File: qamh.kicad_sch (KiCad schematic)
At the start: 18 parts, among them J1 Eurorack_Power_16pin_Shrouded, J2 OUTPUT, J3 INPUT 1, J4 INPUT 2, J5 INPUT 3, J6 Conn_01x02_Pin

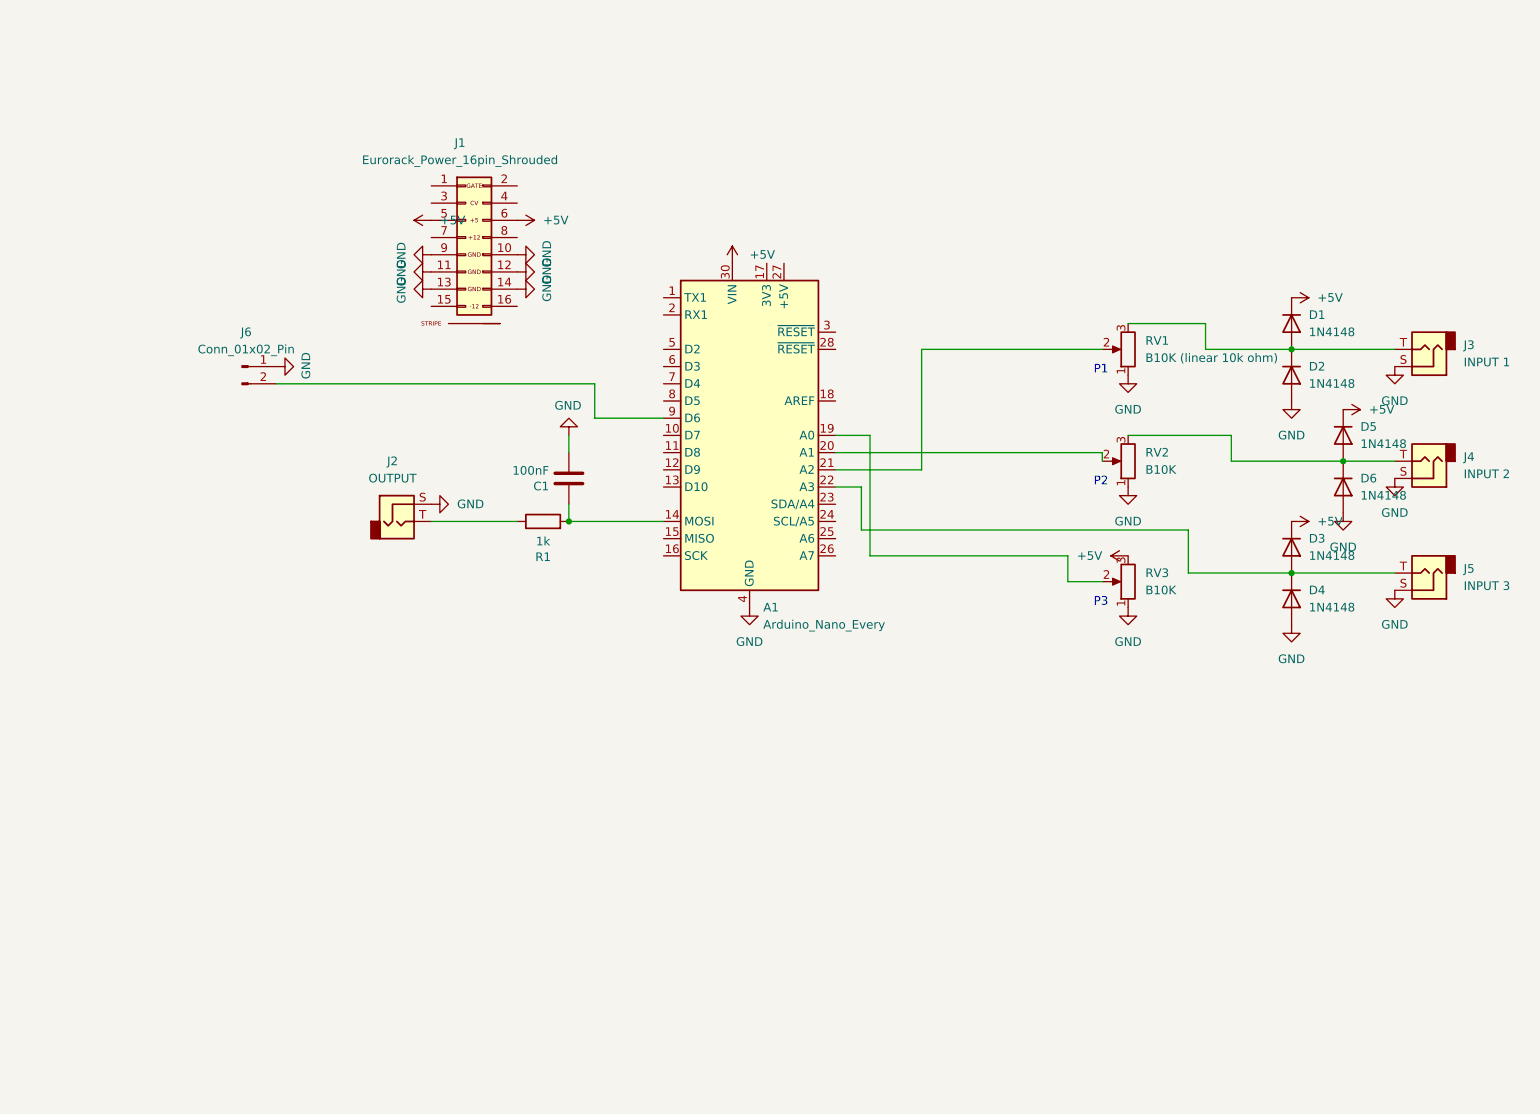
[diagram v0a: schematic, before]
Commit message: replaced nano by pro mini
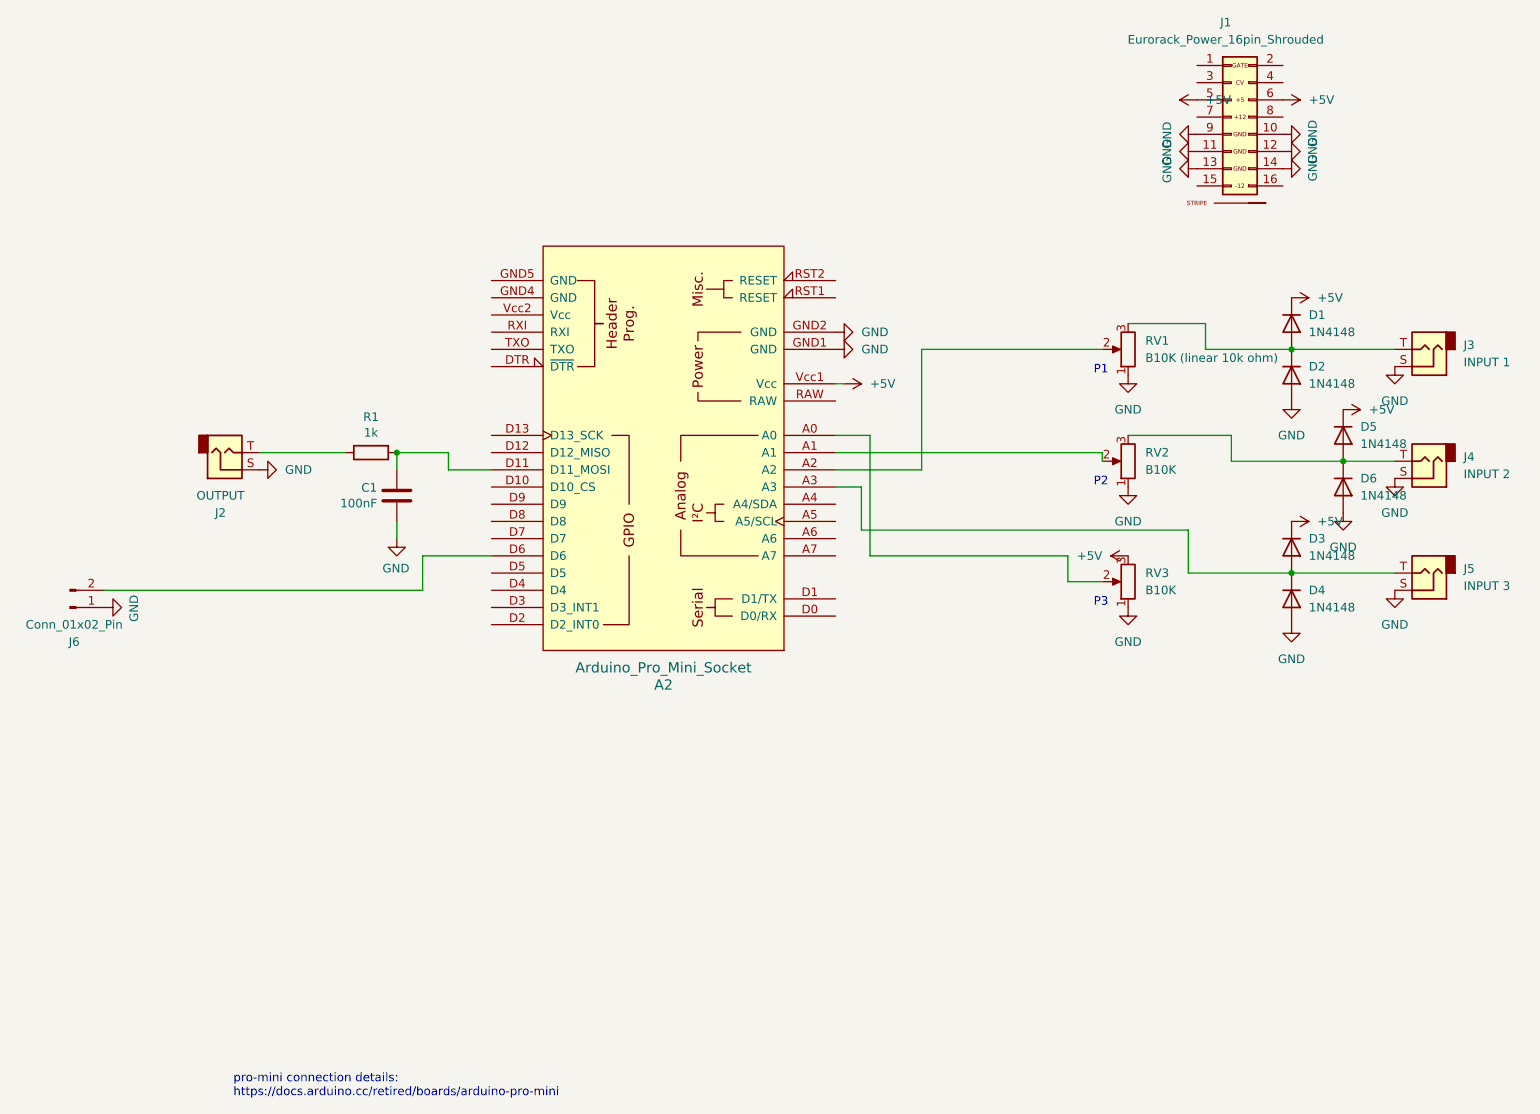
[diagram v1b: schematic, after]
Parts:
- removed A1: Arduino_Nano_Every, Module:Arduino_Nano, symbol MCU_Module:Arduino_Nano_Every
- added A2: Arduino_Pro_Mini_Socket, PCM_arduino-library:Arduino_Pro_Mini_Socket, symbol PCM_:Arduino_Pro_Mini_Socket
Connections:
- net +5V: now also A2.Vcc1 (Vcc)
- net GND: now also A2.GND1 (GND), A2.GND2 (GND)
- net at D3.2 (A), D4.1 (K), J5.T: now also A2.A3
- net at C1.1, R1.2: now also A2.D11 (D11_MOSI)
- net at RV2.2: now also A2.A1
- net at RV1.2: now also A2.A2
- net at RV3.2: now also A2.A0
- net at J6.2 (Pin_2): now also A2.D6
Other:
- note added: "pro-mini connection details: https://docs.arduino.cc/retired/boards/arduino-pro-mini"
- moved on the sheet: C1, J1, J2, J6, R1

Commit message: routing
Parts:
- added R2: 10k, Resistor_THT:R_Axial_DIN0204_L3.6mm_D1.6mm_P7.62mm_Horizontal, symbol Device:R
- added SW1: SW_Push, Button_Switch_THT:SW_PUSH_6mm_H5mm, symbol Switch:SW_Push
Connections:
- net +5V: now also R2.1
- net GND: now also SW1.1
- net at A2.D2 (D2_INT0): now also R2.2, SW1.2
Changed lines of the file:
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@@
   (title_block
     (title "Qamh")
-    (date "2023-10-07")
-    (rev "0.1")
+    (date "2023-10-08")
+    (rev "0.2")
     (company "www.vanheusden.com")
     (comment 1 "https://github.com/folkertvanheusden/qamh/")
@@
   (junction (at 223.52 100.33) (diameter 0) (color 0 0 0 0)
   )
+  (junction (at 100.33 107.95) (diameter 0) (color 0 0 0 0)
+  )
   (junction (at 231.14 83.82) (diameter 0) (color 0 0 0 0)
   )
@@
     (stroke (width 0) (type default))
   )
+  (wire (pts (xy 96.52 107.95) (xy 100.33 107.95))
+    (stroke (width 0) (type default))
+  )
   (wire (pts (xy 95.25 102.87) (xy 95.25 97.79))
     (stroke (width 0) (type default))
   )
+  (wire (pts (xy 100.33 107.95) (xy 100.33 133.35))
+    (stroke (width 0) (type default))
+  )
   (wire (pts (xy 168.91 85.09) (xy 156.21 85.09))
     (stroke (width 0) (type default))
@@
     (stroke (width 0) (type default))
   )
+  (wire (pts (xy 100.33 107.95) (xy 105.41 107.95))
+    (stroke (width 0) (type default))
+  )
   (wire (pts (xy 238.76 100.33) (xy 223.52 100.33))
     (stroke (width 0) (type default))
@@
     (stroke (width 0) (type default))
   )
+  (wire (pts (xy 100.33 133.35) (xy 78.74 133.35))
+    (stroke (width 0) (type default))
+  )
   (wire (pts (xy 223.52 67.31) (xy 210.82 67.31))
     (stroke (width 0) (type default))
@@
   )
   (wire (pts (xy 161.29 97.79) (xy 161.29 80.01))
+    (stroke (width 0) (type default))
+  )
+  (wire (pts (xy 85.09 107.95) (xy 88.9 107.95))
     (stroke (width 0) (type default))
   )
@@
     )
   )
+  (symbol (lib_id "Switch:SW_Push") (at 73.66 133.35 0) (unit 1)
+    (in_bom yes) (on_board yes) (dnp no) (fields_autoplaced)
+    (property "Reference" "SW1" (at 73.66 125.73 0)
+      (effects (font (size 1.27 1.27)))
+    )
+    (property "Value" "SW_Push" (at 73.66 128.27 0)
+      (effects (font (size 1.27 1.27)))
+    )
+    (property "Footprint" "Button_Switch_THT:SW_PUSH_6mm_H5mm" (at 73.66 128.27 0)
+      (effects (font (size 1.27 1.27)) hide)
+    )
+    (property "Datasheet" "~" (at 73.66 128.27 0)
+      (effects (font (size 1.27 1.27)) hide)
+    )
+    (pin "1")
+    (pin "2")
+    (instances
+      (project "qamh"
+        (path "/c13d4df3-e81e-4244-a624-8f3edbb92138"
+          (reference "SW1") (unit 1)
+        )
+      )
+    )
+  )
   (symbol (lib_id "Device:C") (at 91.44 88.9 0) (mirror y) (unit 1)
     (in_bom yes) (on_board yes) (dnp no)
@@
     )
   )
+  (symbol (lib_id "power:GND") (at 68.58 133.35 270) (unit 1)
+    (in_bom yes) (on_board yes) (dnp no) (fields_autoplaced)
+    (property "Reference" "#PWR04" (at 62.23 133.35 0)
+      (effects (font (size 1.27 1.27)) hide)
+    )
+    (property "Value" "GND" (at 64.77 133.35 90)
+      (effects (font (size 1.27 1.27)) (justify right))
+    )
+    (property "Footprint" "" (at 68.58 133.35 0)
+      (effects (font (size 1.27 1.27)) hide)
+    )
+    (property "Datasheet" "" (at 68.58 133.35 0)
+      (effects (font (size 1.27 1.27)) hide)
+    )
+    (pin "1")
+    (instances
+      (project "qamh"
+        (path "/c13d4df3-e81e-4244-a624-8f3edbb92138"
+          (reference "#PWR04") (unit 1)
+        )
+      )
+    )
+  )
   (symbol (lib_id "power:+5V") (at 209.55 30.48 90) (unit 1)
     (in_bom yes) (on_board yes) (dnp no) (fields_autoplaced)
@@
     )
   )
+  (symbol (lib_id "Device:R") (at 92.71 107.95 90) (mirror x) (unit 1)
+    (in_bom yes) (on_board yes) (dnp no)
+    (property "Reference" "R2" (at 92.71 102.6922 90)
+      (effects (font (size 1.27 1.27)))
+    )
+    (property "Value" "10k" (at 92.71 105.0036 90)
+      (effects (font (size 1.27 1.27)))
+    )
+    (property "Footprint" "Resistor_THT:R_Axial_DIN0204_L3.6mm_D1.6mm_P7.62mm_Horizontal" (at 92.71 106.172 90)
+      (effects (font (size 1.27 1.27)) hide)
+    )
+    (property "Datasheet" "~" (at 92.71 107.95 0)
+      (effects (font (size 1.27 1.27)) hide)
+    )
+    (pin "1")
+    (pin "2")
+    (instances
+      (project "qamh"
+        (path "/c13d4df3-e81e-4244-a624-8f3edbb92138"
+          (reference "R2") (unit 1)
+        )
+      )
+    )
+  )
   (symbol (lib_id "Connector:AudioJack2") (at 243.84 83.82 180) (unit 1)
     (in_bom yes) (on_board yes) (dnp no) (fields_autoplaced)
@@
         )
       )
+    )
+  )
+  (symbol (lib_id "power:+5V") (at 85.09 107.95 90) (unit 1)
+    (in_bom yes) (on_board yes) (dnp no) (fields_autoplaced)
+    (property "Reference" "#PWR03" (at 88.9 107.95 0)
+      (effects (font (size 1.27 1.27)) hide)
+    )
+    (property "Value" "+5V" (at 81.28 107.95 90)
+      (effects (font (size 1.27 1.27)) (justify left))
+    )
+    (property "Footprint" "" (at 85.09 107.95 0)
+      (effects (font (size 1.27 1.27)) hide)
+    )
+    (property "Datasheet" "" (at 85.09 107.95 0)
+      (effects (font (size 1.27 1.27)) hide)
+    )
+    (pin "1")
+    (instances
+      (project "qamh"
+        (path "/c13d4df3-e81e-4244-a624-8f3edbb92138"
+          (reference "#PWR03") (unit 1)
+        )
+      )

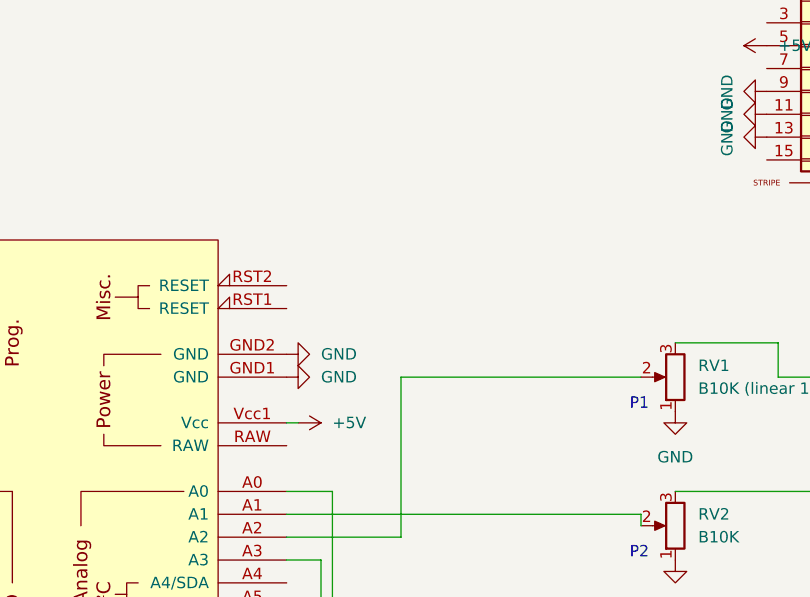
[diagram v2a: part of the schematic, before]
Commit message: header for plug/unplug 5V
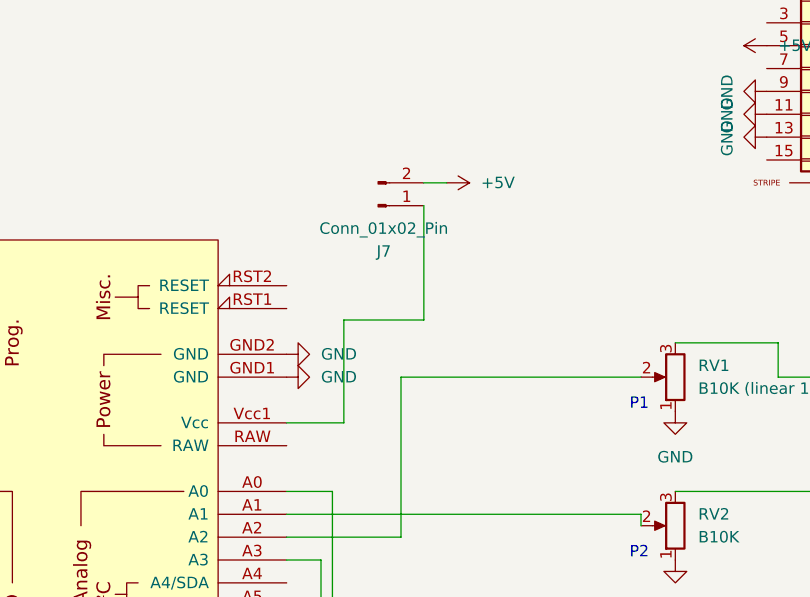
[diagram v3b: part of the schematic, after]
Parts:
- added J7: Conn_01x02_Pin, Connector_PinHeader_2.54mm:PinHeader_1x02_P2.54mm_Vertical, symbol Connector:Conn_01x02_Pin
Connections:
- net +5V: now also J7.2 (Pin_2); no longer A2.Vcc1 (Vcc)
- new net: A2.Vcc1 (Vcc), J7.1 (Pin_1)
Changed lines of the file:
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@@
+    (stroke (width 0) (type default))
+  )
+  (wire (pts (xy 171.45 48.26) (xy 171.45 60.96))
     (stroke (width 0) (type default))
   )
@@
     (stroke (width 0) (type default))
   )
+  (wire (pts (xy 162.56 60.96) (xy 162.56 72.39))
+    (stroke (width 0) (type default))
+  )
   (wire (pts (xy 168.91 67.31) (xy 168.91 85.09))
     (stroke (width 0) (type default))
@@
     (stroke (width 0) (type default))
   )
+  (wire (pts (xy 171.45 45.72) (xy 173.99 45.72))
+    (stroke (width 0) (type default))
+  )
   (wire (pts (xy 100.33 107.95) (xy 100.33 133.35))
     (stroke (width 0) (type default))
@@
     (stroke (width 0) (type default))
   )
+  (wire (pts (xy 171.45 60.96) (xy 162.56 60.96))
+    (stroke (width 0) (type default))
+  )
   (wire (pts (xy 238.76 100.33) (xy 223.52 100.33))
     (stroke (width 0) (type default))
@@
     (stroke (width 0) (type default))
   )
-  (wire (pts (xy 156.21 72.39) (xy 157.48 72.39))
+  (wire (pts (xy 156.21 72.39) (xy 162.56 72.39))
     (stroke (width 0) (type default))
   )
@@
     )
   )
-  (symbol (lib_id "power:+5V") (at 157.48 72.39 270) (unit 1)
-    (in_bom yes) (on_board yes) (dnp no) (fields_autoplaced)
-    (property "Reference" "#PWR01" (at 153.67 72.39 0)
-      (effects (font (size 1.27 1.27)) hide)
-    )
-    (property "Value" "+5V" (at 161.29 72.39 90)
-      (effects (font (size 1.27 1.27)) (justify left))
-    )
-    (property "Footprint" "" (at 157.48 72.39 0)
-      (effects (font (size 1.27 1.27)) hide)
-    )
-    (property "Datasheet" "" (at 157.48 72.39 0)
-      (effects (font (size 1.27 1.27)) hide)
-    )
-    (pin "1")
-    (instances
-      (project "qamh"
-        (path "/c13d4df3-e81e-4244-a624-8f3edbb92138"
-          (reference "#PWR01") (unit 1)
-        )
-      )
-    )
-  )
   (symbol (lib_id "power:GND") (at 199.39 105.41 0) (unit 1)
     (in_bom yes) (on_board yes) (dnp no) (fields_autoplaced)
@@
         )
       )
+    )
+  )
+  (symbol (lib_id "Connector:Conn_01x02_Pin") (at 166.37 48.26 0) (mirror x) (unit 1)
+    (in_bom yes) (on_board yes) (dnp no) (fields_autoplaced)
+    (property "Reference" "J7" (at 167.005 53.34 0)
+      (effects (font (size 1.27 1.27)))
+    )
+    (property "Value" "Conn_01x02_Pin" (at 167.005 50.8 0)
+      (effects (font (size 1.27 1.27)))
+    )
+    (property "Footprint" "Connector_PinHeader_2.54mm:PinHeader_1x02_P2.54mm_Vertical" (at 166.37 48.26 0)
+      (effects (font (size 1.27 1.27)) hide)
+    )
+    (property "Datasheet" "~" (at 166.37 48.26 0)
+      (effects (font (size 1.27 1.27)) hide)
+    )
+    (pin "1")
+    (pin "2")
+    (instances
+      (project "qamh"
+        (path "/c13d4df3-e81e-4244-a624-8f3edbb92138"
+          (reference "J7") (unit 1)
+        )
+      )
+    )
+  )
+  (symbol (lib_id "power:+5V") (at 173.99 45.72 270) (unit 1)
+    (in_bom yes) (on_board yes) (dnp no) (fields_autoplaced)
+    (property "Reference" "#PWR01" (at 170.18 45.72 0)
+      (effects (font (size 1.27 1.27)) hide)
+    )
+    (property "Value" "+5V" (at 177.8 45.72 90)
+      (effects (font (size 1.27 1.27)) (justify left))
+    )
+    (property "Footprint" "" (at 173.99 45.72 0)
+      (effects (font (size 1.27 1.27)) hide)
+    )
+    (property "Datasheet" "" (at 173.99 45.72 0)
+      (effects (font (size 1.27 1.27)) hide)
+    )
+    (pin "1")
+    (instances
+      (project "qamh"
+        (path "/c13d4df3-e81e-4244-a624-8f3edbb92138"
+          (reference "#PWR01") (unit 1)
+        )
+      )
